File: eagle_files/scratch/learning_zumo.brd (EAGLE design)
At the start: 66 x 66 mm, 68 parts, among them U1 5v, U2 3v3

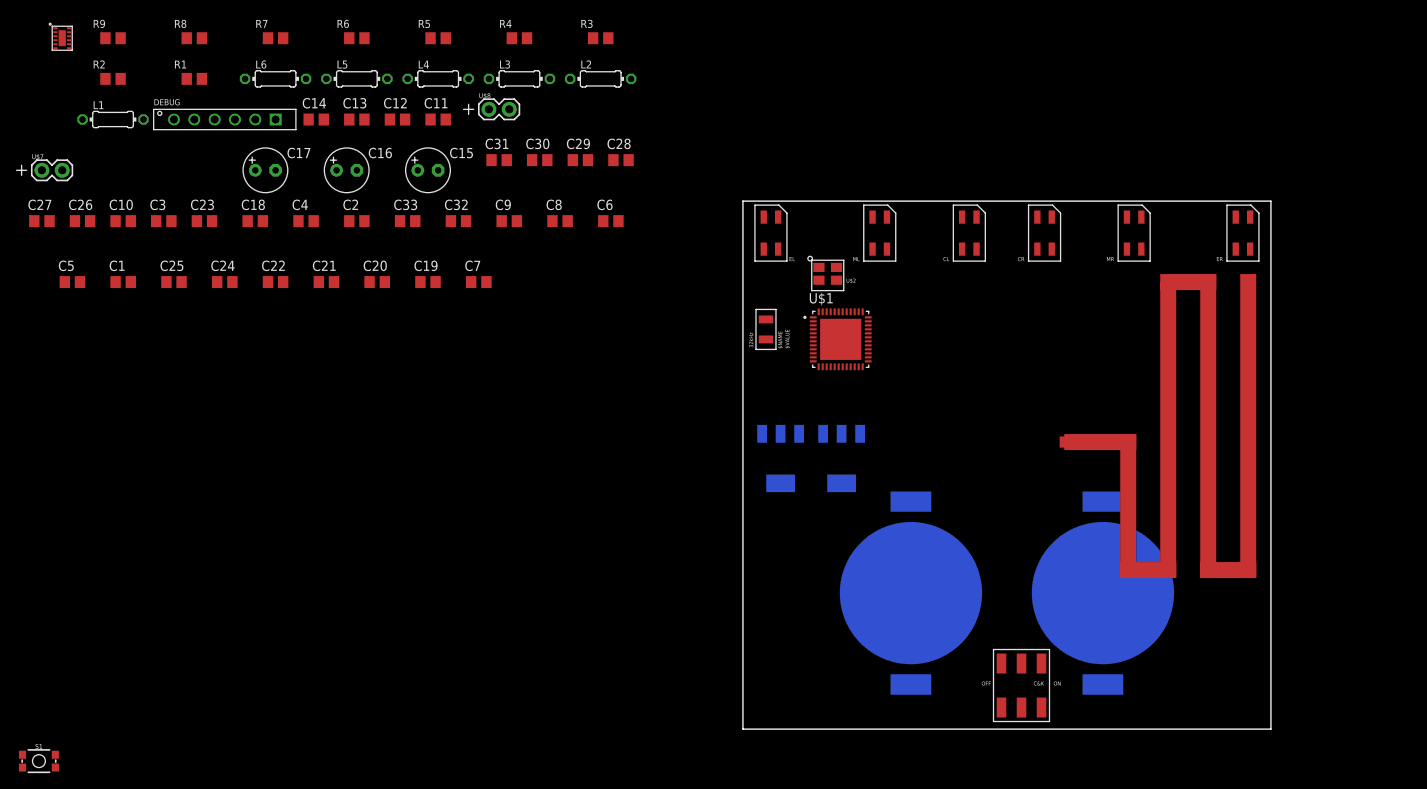
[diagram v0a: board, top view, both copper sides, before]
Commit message: figuring last details on antenna balun
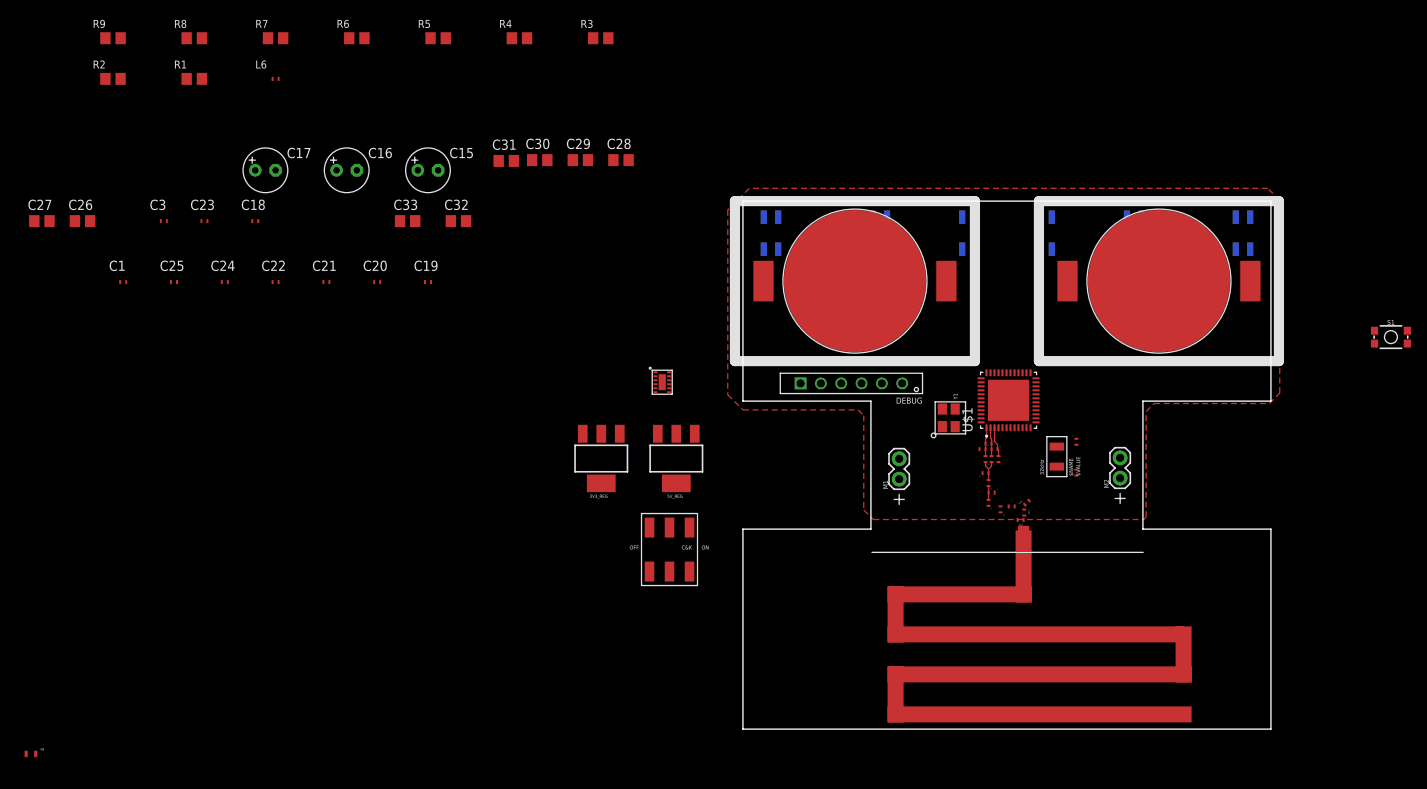
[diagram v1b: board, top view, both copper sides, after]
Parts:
- removed 32KHZ: CRYSTAL-32KHZ, Swarm:CRYSTAL-32KHZ
- removed U$2: CRYSTAL-24MHZ, Swarm:CRYSTAL-24MHZ
- removed U$4: DEBUG_BREAKOUT, CC1310F128RGZ:DEBUG_BREAKOUT
- removed U$5: DRV8835DRV8835, Swarm:DRV8835
- removed U$6: SWITCH_JS202011SCQN, Swarm:SWITCH_JS202011SCQN
- removed U$7, U$8: DC_MOTOR, Swarm:1X02
- removed U1: 5v, Swarm:NU32V7_SOT223
- removed U2: 3v3, Swarm:NU32V7_SOT223
- added 3V3_REG: 3v3, Swarm:NU32V7_SOT223
- added 5V_REG: 5v, Swarm:NU32V7_SOT223
- added DEBUG_HEADER: DEBUG_BREAKOUT, CC1310F128RGZ:DEBUG_BREAKOUT
- added DRV8835: DRV8835DRV8835, Swarm:DRV8835
- added FB: FERRITE_BEAD, CC1310F128RGZ:FERRITE_BEAD
- added M1, M2: DC_MOTOR, Swarm:1X02
- added PW_SW: SWITCH_JS202011SCQN, Swarm:SWITCH_JS202011SCQN
- added Y1: CRYSTAL-24MHZ, Swarm:CRYSTAL-24MHZ
- added Y2: CRYSTAL-32KHZ, Swarm:CRYSTAL-32KHZ
- C1: value 0,1uF -> 100nF; device Swarm:C0805 -> learning_particle:C0402_US
- C10, C18, C19, C2, C20, C21, C22, C23, C24, C25, C3, C4, C5, C6, C7, C8, C9: device Swarm:C0805 -> learning_particle:C0402_US
- C11: value (none) -> 100pF; device Swarm:C0805 -> learning_particle:C0402_US
- C12, C14: value (none) -> DNM; device Swarm:C0805 -> learning_particle:C0402_US
- C13: value (none) -> 1.8pF; device Swarm:C0805 -> learning_particle:C0402_US
- L1, L2, L3, L4, L5, L6: device Swarm:0204/7 -> learning_particle:L0402_US
- U$1: device CC1310F128RGZT:QFN50P700X700X100-49N -> learning_particle:QFN50P700X700X100-49N
- moved S1 177.1 mm to (81.0, 49.0)
- moved L1 116.7 mm to (30.7, 35.7)
- moved C5 115.7 mm to (29.9, 35.0)
- moved C10 115.4 mm to (32.2, 27.5), turned to 270 degrees
- moved C4 101.3 mm to (41.7, 32.1), turned to 270 degrees
- moved C14 101.3 mm to (34.7, 26.1), turned to 180 degrees
- moved C13 96.8 mm to (35.2, 27.1), turned to 270 degrees
- moved L5 95.1 mm to (30.7, 28.3), turned to 270 degrees
- moved C2 94.1 mm to (41.7, 35.9), turned to 90 degrees
- moved C12 92.1 mm to (35.5, 28.3), turned to 45 degrees
- moved C11 86.5 mm to (33.6, 27.8)
- moved L4 85.4 mm to (30.7, 30.8), turned to 270 degrees
- moved L3 75.3 mm to (31.4, 35.0)
- moved C9 69.2 mm to (31.1, 29.6)
- moved C7 68.6 mm to (31.9, 33.8), turned to 270 degrees
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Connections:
- removed net N$10: C7.1, L3.2, U$1.3
- removed net N$11: U$1.47, U$2.Q1
- removed net N$13: C9.1, L4.2, L5.1
- removed net N$14: C10.1, C11.1, L5.2
- removed net N$22: U$1.31
- removed net N$7 (its old number): U$1.42
- removed net N$8: U$1.43
- removed net N$9: 32KHZ.Q2, C4.1, U$1.5
- new net RF_N: C6.1, L1.P$2, L3.P$1, U$1.2
- new net RF_P: C5.2, L1.P$1, L2.P$1, U$1.1
- new net RF_TX: C7.1, L3.P$2, U$1.3
- new net X32_Q1: C2.1, U$1.4, Y2.Q1
- new net X32_Q2: C4.1, U$1.5, Y2.Q2
- new net X_48_Q1: U$1.46, Y1.Q2
- new net X_48_Q2: U$1.47, Y1.Q1
- net 3V3: now also 3V3_REG.OUTPUT, 3V3_REG.VOUT, DRV8835.12.VCC, PW_SW.1.COMM; no longer U$5.12.VCC, U$6.1.COMM, U2.OUTPUT, U2.VOUT
- net 5V: now also 3V3_REG.INPUT, 5V_REG.OUTPUT, 5V_REG.VOUT, DRV8835.11.MODE; no longer U$5.11.MODE, U1.OUTPUT, U1.VOUT, U2.INPUT
- net DCDC_SW: now also L6.P$1; no longer L6.1
- net GND: now also 3V3_REG.GND, 5V_REG.GND, DEBUG_HEADER.GND, DRV8835.13.GND, DRV8835.6.GND, Y1.GND, Y1.GND2; no longer U$2.GND, U$2.GND2, U$4.GND, U$5.13.GND, U$5.6.GND, U1.GND, U2.GND
- net JTAG_TCK: now also DEBUG_HEADER.TCK; no longer U$4.TCK
- net JTAG_TDI: now also DEBUG_HEADER.TDI; no longer U$4.TDI
- net JTAG_TDO: now also DEBUG_HEADER.TDO; no longer U$4.TDO
- net JTAG_TMS: now also DEBUG_HEADER.TMS; no longer U$4.TMS
- net M1DIR: now also DRV8835.10.A_PHASE; no longer U$5.10.A_PHASE
- net M1PWM: now also DRV8835.9.A_ENBL; no longer U$5.9.A_ENBL
- net M2DIR: now also DRV8835.8.B_PHASE; no longer U$5.8.B_PHASE
- net M2PWM: now also DRV8835.7.B_ENBL; no longer U$5.7.B_ENBL
- net N$1: no longer 32KHZ.Q1, C2.1, U$1.10, U$1.11, U$1.12, U$1.14, U$1.15, U$1.4, U$1.6, U$1.7, U$1.8, U$1.9
- net N$12: now also L2.P$2, L4.P$1; no longer L2.2, L4.1
- net N$2: now also C9.1, L4.P$2, L5.P$1; no longer C5.2, C6.1, L1.1, L1.2, L2.1, L3.1, U$1.1, U$1.2, U$1.28, U$1.32, U$1.46, U$2.Q2
- net N$24: now also DRV8835.5.BOUT+, M2.1; no longer U$5.5.BOUT+, U$7.1
- net N$25: now also DRV8835.4.BOUT-, M2.2; no longer U$5.4.BOUT-, U$7.2
- net N$26: now also DRV8835.3.AOUT+, M1.1; no longer U$5.3.AOUT+, U$8.1
- net N$27: now also DRV8835.2.AOUT-, M1.2; no longer U$5.2.AOUT-, U$8.2
- net N$3: now also C10.1, C11.1, L5.P$2; no longer U$1.16
- net N$4: now also FB.P$1, PW_SW.3.IN2; no longer U$1.19, U$1.20, U$1.21
- net N_RESET: now also DEBUG_HEADER.RESET; no longer U$4.RESET
- net VBAT: now also 5V_REG.INPUT, DRV8835.1.VM; no longer U$5.1.VM, U1.INPUT
- net VDDR: now also L6.P$2; no longer L6.2
- net VDDS: now also FB.P$2; no longer U$6.3.IN2
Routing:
- net RF_TX: track 0.00 -> 3.94 mm
- net RF_P: track 0.00 -> 3.59 mm
- net RF_N: track 0.00 -> 3.59 mm
- net N$12: track 0.00 -> 3.43 mm
- net N$2: track 0.00 -> 1.73 mm
- added copper zone on layer 1, net GND
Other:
- outline, holes or cut-outs redrawn

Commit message: most updated, finished balun and other minimum reqs for CC1310, working on integrating battery motor driver and sensors
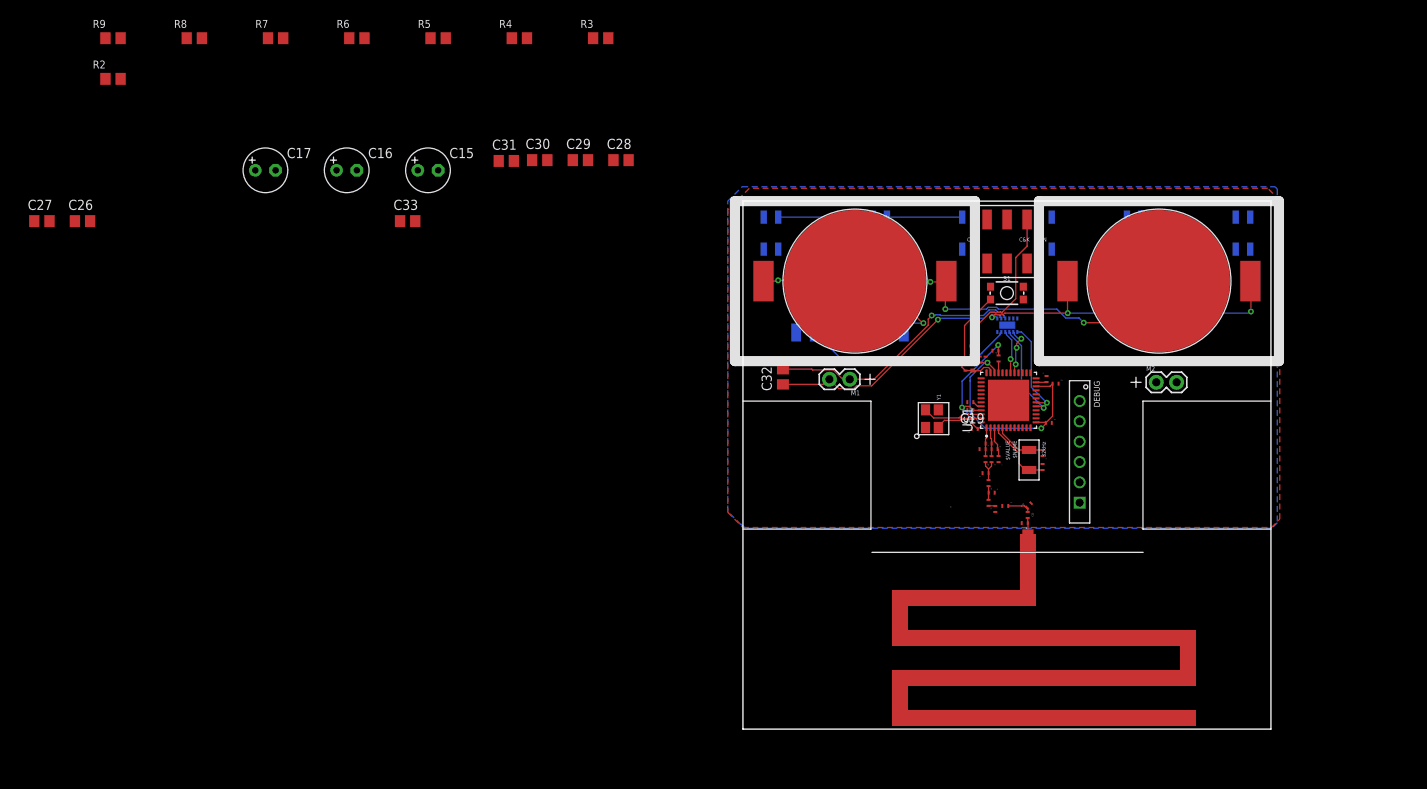
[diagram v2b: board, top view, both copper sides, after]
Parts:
- C18: value 34nF -> 22nF
- R1: device Swarm:R0805 -> learning_particle:R0402_US
- R2, R6: value 220 -> 147
- moved FB 128.0 mm to (28.7, 47.3), turned to 270 degrees
- moved C3 112.1 mm to (38.0, 43.8), turned to 90 degrees
- moved C1 105.8 mm to (27.8, 45.2), turned to 90 degrees
- moved R1 103.7 mm to (28.7, 45.3), turned to 90 degrees
- moved C25 100.8 mm to (28.4, 39.9), turned to 180 degrees
- moved C23 100.2 mm to (31.6, 47.3), turned to 180 degrees
- moved L6 96.9 mm to (31.9, 46.3), turned to 90 degrees
- moved C24 95.5 mm to (29.0, 37.5), turned to 180 degrees
- moved C18 92.2 mm to (29.6, 46.2), turned to 90 degrees
- moved C21 92.0 mm to (38.2, 38.3)
- moved C22 89.3 mm to (30.3, 46.2), turned to 90 degrees
- moved C20 85.7 mm to (39.1, 43.2)
- moved C19 69.4 mm to (28.4, 40.9), turned to 180 degrees
- moved PW_SW 57.1 mm to (33.0, 61.0)
- moved S1 48.3 mm to (33.0, 54.5)
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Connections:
- net 5V: now also R2.2, R6.2
- net N_RESET: now also R1.P$1; no longer R1.1
- net VBAT: no longer R2.2, R6.2
- net VDDS: now also R1.P$2; no longer R1.2
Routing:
- net N$5: track 0.00 -> 58.2 mm, vias 0 -> 4
- net VBAT: track 0.00 -> 41.7 mm, vias 0 -> 3
- net N$26: track 0.00 -> 33.0 mm, vias 0 -> 1
- net 5V: track 0.00 -> 32.9 mm, vias 0 -> 2
- net N$27: track 0.00 -> 32.8 mm, vias 0 -> 1
- net VDDS: track 0.00 -> 31.4 mm, vias 0 -> 2
- net N$4: track 0.00 -> 19.5 mm
- net VDDR: track 0.00 -> 18.5 mm, vias 0 -> 3
- net N_RESET: track 0.00 -> 14.4 mm
- net GND: track 0.00 -> 13.7 mm, vias 0 -> 1
- net M1PWM: track 0.00 -> 12.3 mm, vias 0 -> 1
- net M2PWM: track 0.00 -> 12.1 mm, vias 0 -> 1
- net N$20: track 0.00 -> 11.8 mm
- net N$21: track 0.00 -> 9.40 mm
- net X32_Q1: track 0.00 -> 8.81 mm
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- added copper zone on layer 16, net GND
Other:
- outline, holes or cut-outs redrawn

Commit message: finished up iteration 1 of the board!
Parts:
- removed C16, C17: (no value), Swarm:E2,5-6
- added U$2: GP2Y_DIST_SENSE_BREAKOUT, learning_particle:1X03
- DRV8835: device Swarm:DRV8835 -> learning_particle:DRV8835
- moved R9 122.5 mm to (41.4, 62.5), flipped to the bottom, turned to 90 degrees
- moved R8 117.1 mm to (45.8, 61.4), flipped to the bottom, turned to 270 degrees
- moved R7 115.6 mm to (54.7, 62.6), flipped to the bottom, turned to 90 degrees
- moved R6 110.2 mm to (59.3, 62.7), flipped to the bottom, turned to 270 degrees
- moved C27 108.2 mm to (20.6, 61.7), flipped to the bottom, turned to 270 degrees
- moved C33 103.0 mm to (59.2, 44.0), turned to 270 degrees
- moved C26 91.6 mm to (9.00, 61.7), flipped to the bottom, turned to 270 degrees
- moved R2 87.9 mm to (6.92, 61.7), flipped to the bottom, turned to 270 degrees
- moved C29 77.8 mm to (57.0, 62.6), flipped to the bottom, turned to 270 degrees
- moved C31 73.6 mm to (43.6, 62.6), flipped to the bottom, turned to 90 degrees
- moved R5 73.5 mm to (31.2, 61.7), flipped to the bottom, turned to 90 degrees
- moved C30 72.5 mm to (45.7, 57.3), flipped to the bottom, turned to 90 degrees
- moved R4 56.4 mm to (22.8, 61.7), flipped to the bottom, turned to 90 degrees
- moved C28 49.4 mm to (33.2, 61.7), flipped to the bottom, turned to 90 degrees
- moved C15 47.2 mm to (3.27, 49.6), flipped to the bottom
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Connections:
- new net DIST0: U$1.42, U$2.SIG
- new net N$9: U$1.43
- net 3V3: now also U$2.VCC; no longer C17.+
- net 5V: no longer C16.+
- net GND: now also U$2.GND; no longer C16.-, C17.-
- net IR_CL: now also U$1.39; no longer U$1.37
- net IR_ER: now also U$1.38; no longer U$1.40
- net IR_ML: now also U$1.40; no longer U$1.39
- net IR_MR: now also U$1.37; no longer U$1.38
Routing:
- net 5V: track 32.9 -> 145.8 mm, vias 2 -> 4
- net 3V3: track 6.20 -> 71.8 mm, vias 0 -> 2
- net IR_ER: track 0.00 -> 50.2 mm, vias 0 -> 1
- net IR_MR: track 0.00 -> 40.6 mm, vias 0 -> 1
- net IR_EL: track 0.00 -> 39.6 mm, vias 0 -> 1
- net GND: track 13.7 -> 45.2 mm, vias 1 -> 7
- net N$25: track 0.00 -> 31.1 mm
- net IR_CR: track 0.00 -> 30.9 mm, vias 0 -> 1
- net N$24: track 0.00 -> 30.7 mm
- net VBAT: track 41.7 -> 72.3 mm, vias 3 -> 7
- net IR_ML: track 0.00 -> 27.5 mm, vias 0 -> 1
- net N_RESET: track 14.4 -> 41.0 mm, vias 0 -> 2
- net IR_CL: track 0.00 -> 24.4 mm, vias 0 -> 1
- net JTAG_TDO: track 0.00 -> 22.4 mm
- net JTAG_TDI: track 0.00 -> 19.9 mm
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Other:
- board size 66 x 66 mm -> 66 x 66.4 mm

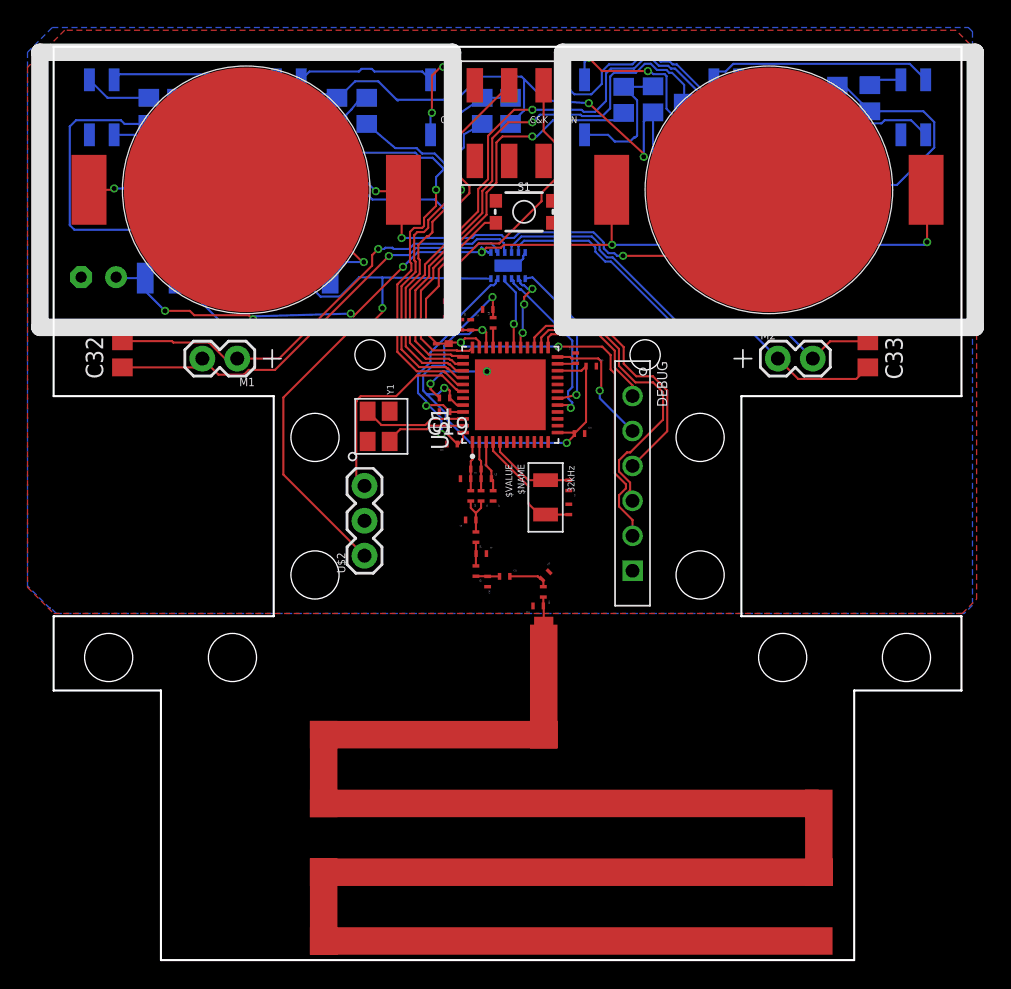
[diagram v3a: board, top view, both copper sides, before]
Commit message: finialized board pre submitting, added vias between top and bottom trace of antenna
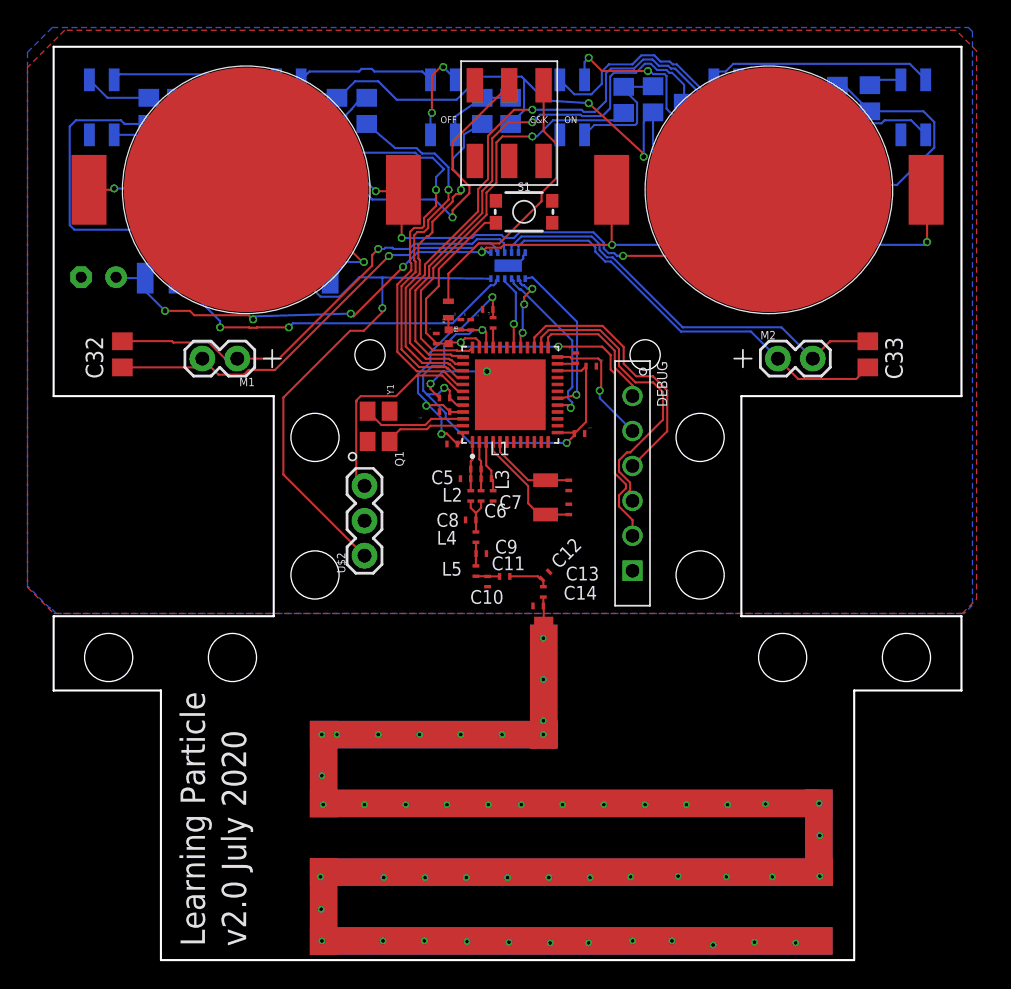
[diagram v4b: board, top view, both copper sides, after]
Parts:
- M1, M2: device Swarm:1X02 -> learning_particle:1X02
- U$10, U$9: device Swarm:20MM_COINCELL -> learning_particle:20MM_COINCELL
- U$3: device CC1310F128RGZ:ANTENNA -> learning_particle:ANTENNA
- Y1: device Swarm:CRYSTAL-24MHZ -> learning_particle:CRYSTAL-24MHZ
- Y2: device Swarm:CRYSTAL-32KHZ -> learning_particle:CRYSTAL-32KHZ
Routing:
- net N$34: track 10.3 -> 9.38 mm
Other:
- board text added: "Learning Particle"
- board text added: "v2.0 July 2020"
